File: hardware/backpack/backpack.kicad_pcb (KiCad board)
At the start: 4 copper layers, 31.7 x 110 mm, 99 parts, among them J1 Conn_01x15, J2 Conn_02x06_Top_Bottom, J3 Conn_02x06_Top_Bottom, J4 AUDIO JACK PJ-324M0, J5 AUDIO JACK PJ-324M0, J6 CONN 2x5 P=2.54mm, J7 USB_C, J8 MICROMOD-2222, J9 USB_C, Q2 2N7002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

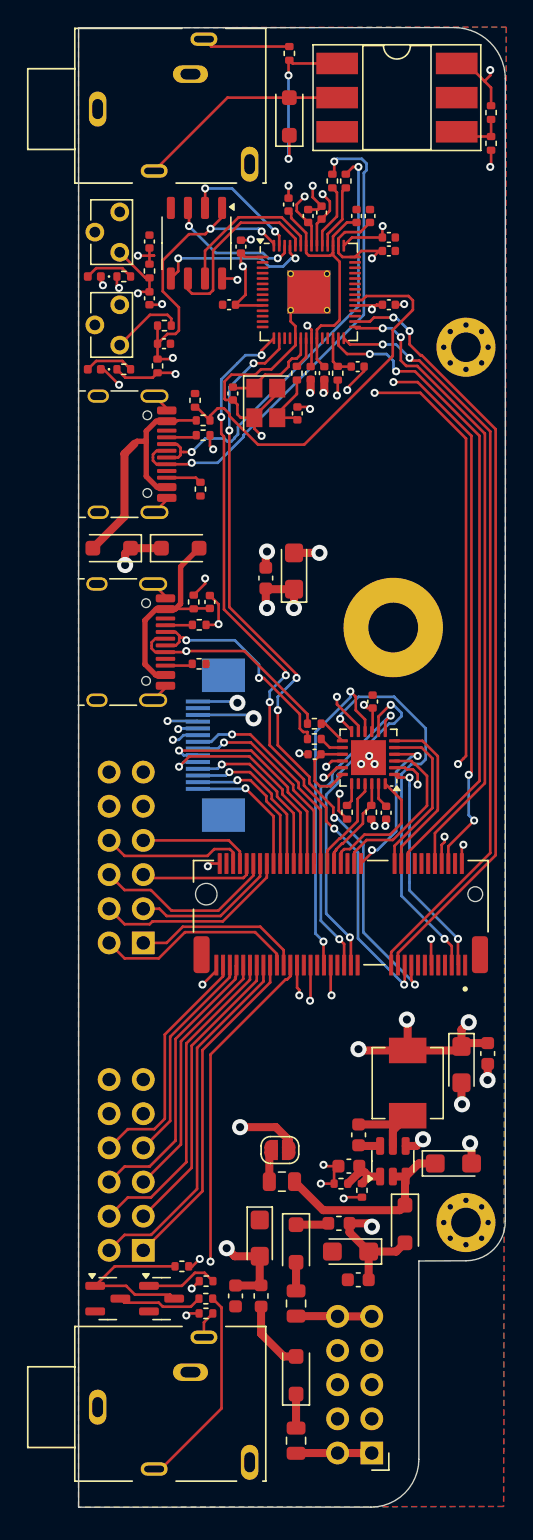
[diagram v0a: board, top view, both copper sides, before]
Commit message: clean up some routing
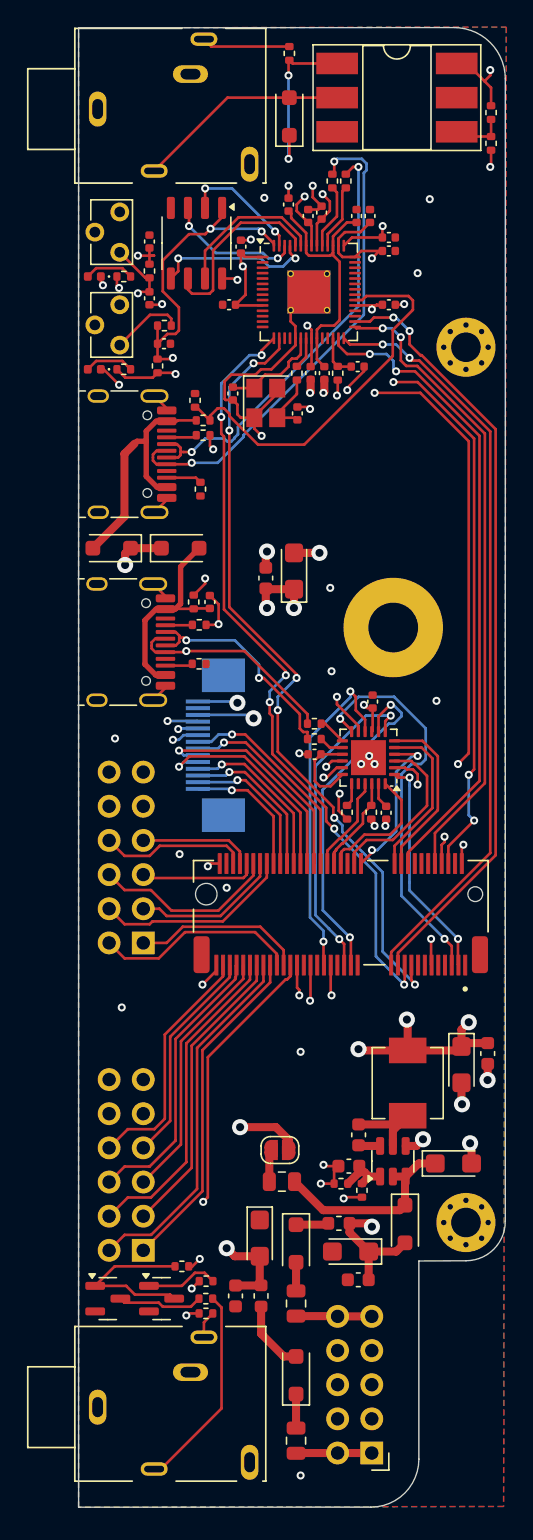
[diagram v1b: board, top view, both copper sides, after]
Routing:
- net ECP5_A5: track 23.1 -> 24.2 mm
- net GND: vias 28 -> 40

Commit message: add some silk designators
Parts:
- added REF**: WEEE-Logo_5.6x8mm_SilkScreen, Symbol:WEEE-Logo_5.6x8mm_SilkScreen, B.Cu at (12.3, 72.7)
- added REF**: OSHW-Symbol_6.7x6mm_SilkScreen, Symbol:OSHW-Symbol_6.7x6mm_SilkScreen, B.Cu at (23.2, 34.0)
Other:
- board text added: "+12"
- board text added: "+3.3V⇦"
- board text added: "-12"
- board text added: "CERN-OHL-S V2"
- board text added: "GND"
- board text added: "JTAG"
- board text added: "OPEN HARDWARE"
- board text added: "RoHS"
- board text added: "ULPI"
- board text added: "VIN // USB"
- board text added: "~{BOOTSEL}"
- board text added: "~{RED!}"

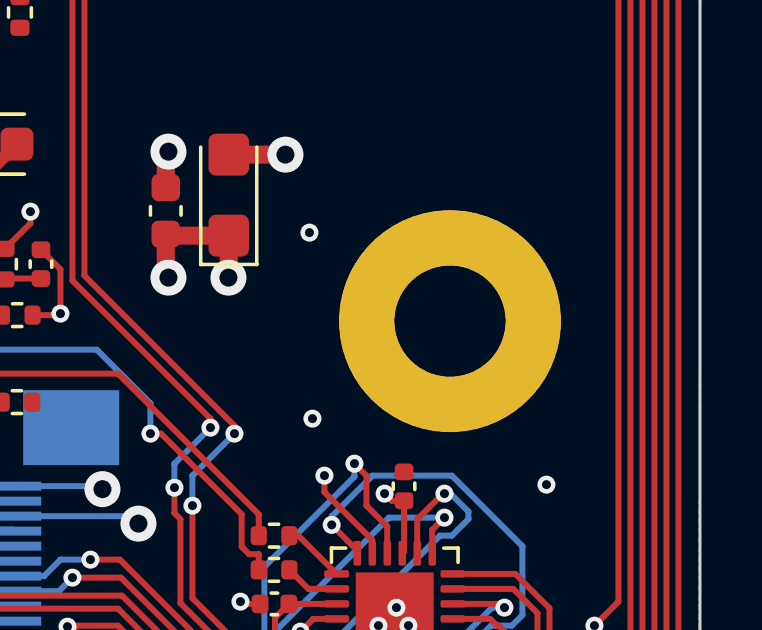
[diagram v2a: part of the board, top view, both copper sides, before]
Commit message: tiliqua, m.2 footprint move/fix, lcsc# for m.2
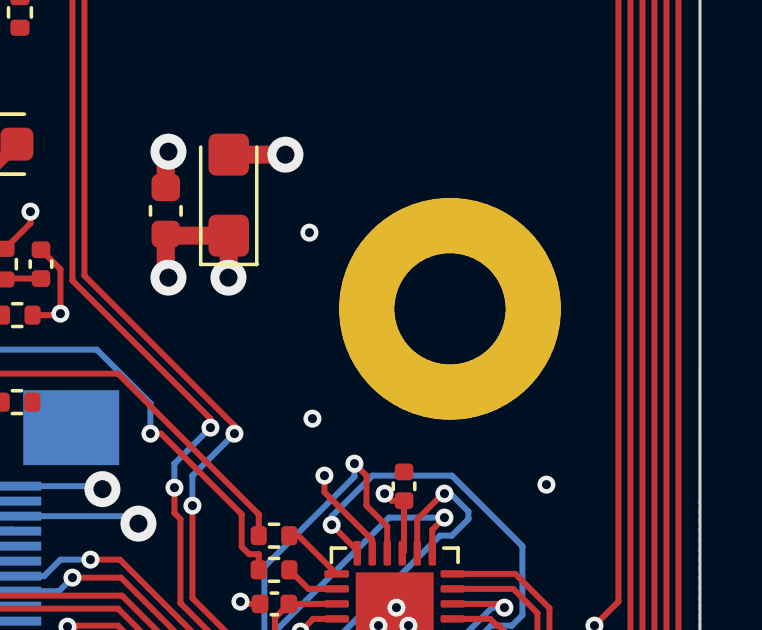
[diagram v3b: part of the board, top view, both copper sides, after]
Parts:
- added G***: LOGO, LOGO, B.Cu at (21.9, 10.3)
- moved REF** 0.41 mm to (23.3, 44.2)
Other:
- board text added: "TILIQUA"
- board text added: "apfelaudio"
- board text removed: "LOGIKEET"
- board text removed: "proto1"
